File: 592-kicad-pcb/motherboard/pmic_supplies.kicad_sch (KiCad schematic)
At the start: 10 parts, among them U21 MICROCHIP TC1304-VI0EMF, U22 LT1761ES5-BYPTRMPBF

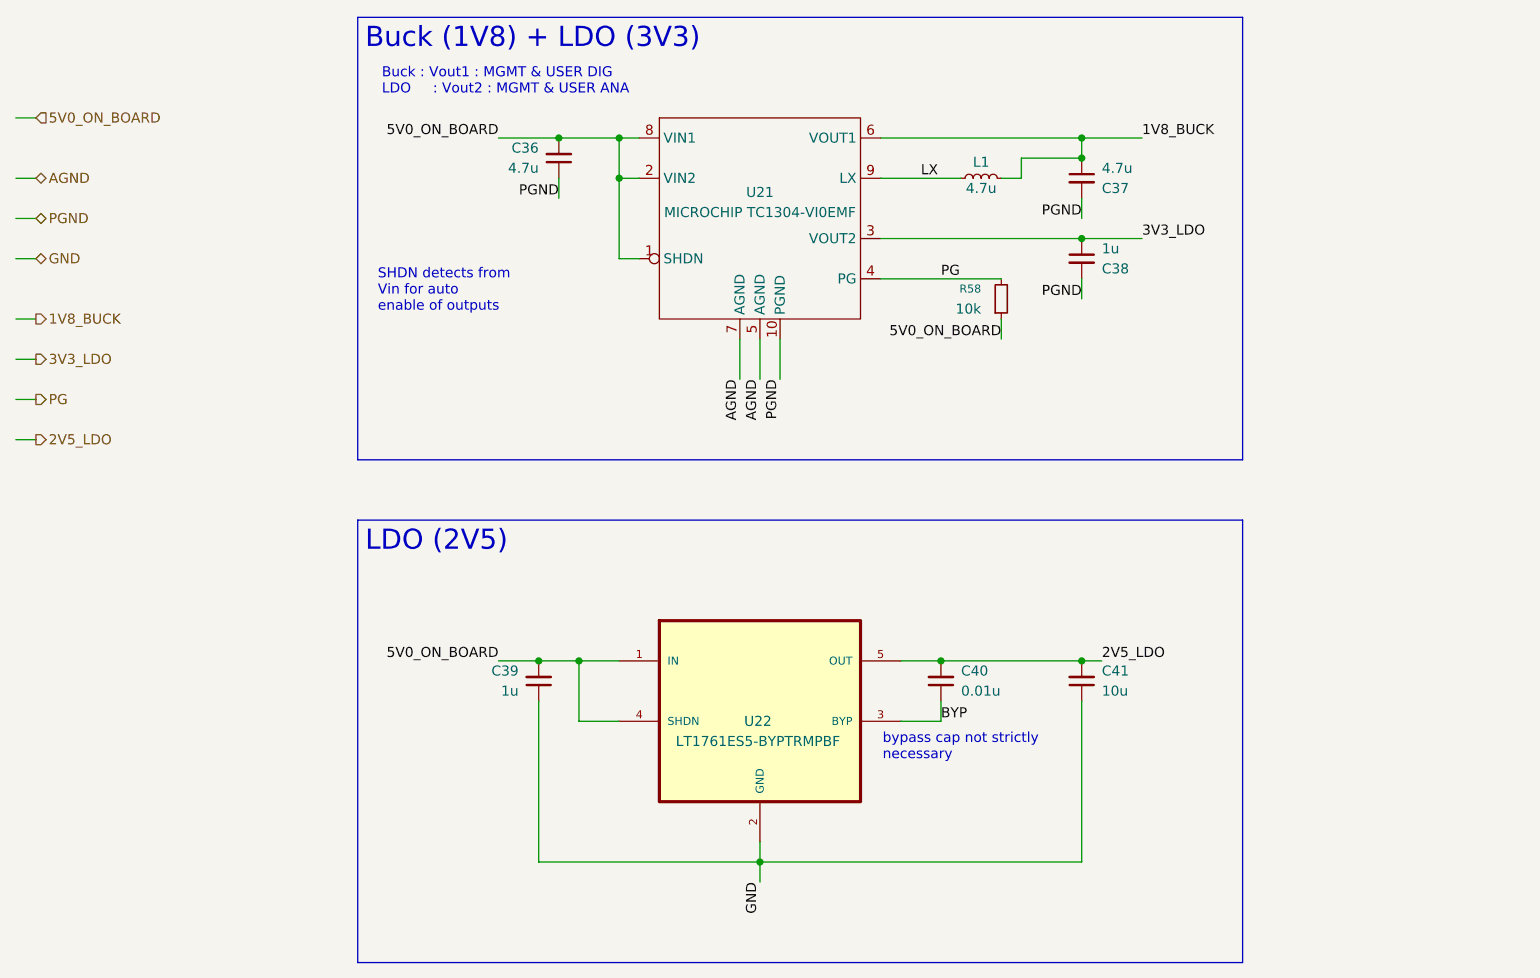
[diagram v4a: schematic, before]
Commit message: fuses, ferrite bead, 5V0 selection connector
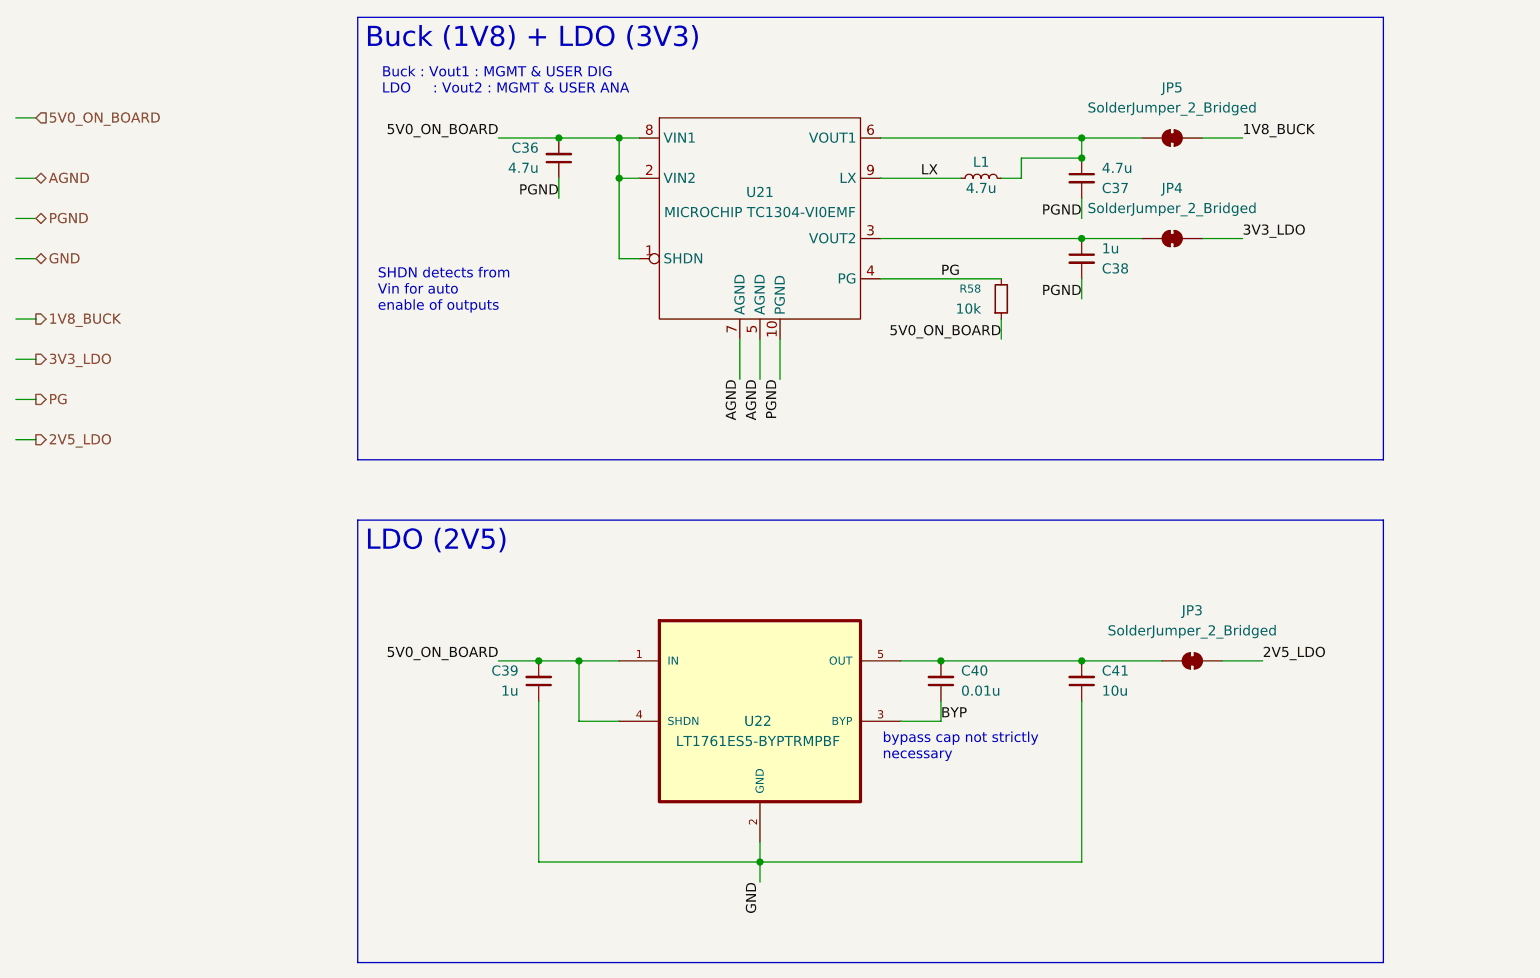
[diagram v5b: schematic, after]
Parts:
- added JP3, JP4, JP5: SolderJumper_2_Bridged, Jumper:SolderJumper-2_P1.3mm_Bridged2Bar_Pad1.0x1.5mm, symbol Jumper:SolderJumper_2_Bridged
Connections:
- net 1V8_BUCK: now also JP5.2 (B); no longer C37.1, L1.2, U21.6 (VOUT1)
- net 2V5_LDO: now also JP3.2 (B); no longer C40.2, C41.2, U22.5 (OUT)
- net 3V3_LDO: now also JP4.2 (B); no longer C38.1, U21.3 (VOUT2)
- new net: C40.2, C41.2, JP3.1 (A), U22.5 (OUT)
- new net: C37.1, JP5.1 (A), L1.2, U21.6 (VOUT1)
- new net: C38.1, JP4.1 (A), U21.3 (VOUT2)
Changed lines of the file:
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@@
 		(exclude_from_sim no)
 		(at 63.5 86.36 0)
-		(size 111.76 55.88)
+		(size 129.54 55.88)
 		(margins 0.9525 0.9525 0.9525 0.9525)
 		(stroke
@@
 		(exclude_from_sim no)
 		(at 63.5 22.86 0)
-		(size 111.76 55.88)
+		(size 129.54 55.88)
 		(margins 0.9525 0.9525 0.9525 0.9525)
 		(stroke
@@
 	(wire
 		(pts
+			(xy 172.72 104.14) (xy 177.8 104.14)
+		)
+		(stroke
+			(width 0)
+			(type default)
+		)
+	)
+	(wire
+		(pts
 			(xy 91.44 104.14) (xy 91.44 111.76)
 		)
@@
 	(wire
 		(pts
-			(xy 154.94 104.14) (xy 157.48 104.14)
+			(xy 154.94 104.14) (xy 165.1 104.14)
 		)
 		(stroke
@@
 	(wire
 		(pts
+			(xy 170.18 50.8) (xy 175.26 50.8)
+		)
+		(stroke
+			(width 0)
+			(type default)
+		)
+	)
+	(wire
+		(pts
 			(xy 96.52 53.34) (xy 99.06 53.34)
 		)
@@
 	(wire
 		(pts
+			(xy 170.18 38.1) (xy 175.26 38.1)
+		)
+		(stroke
+			(width 0)
+			(type default)
+		)
+	)
+	(wire
+		(pts
 			(xy 129.54 50.8) (xy 154.94 50.8)
 		)
@@
 	)
 	(label "3V3_LDO"
-		(at 162.56 50.8 0)
+		(at 175.26 50.8 0)
 		(effects
 			(font
@@
 	)
 	(label "2V5_LDO"
-		(at 157.48 104.14 0)
+		(at 177.8 104.14 0)
 		(effects
 			(font
@@
 	)
 	(label "1V8_BUCK"
-		(at 162.56 38.1 0)
+		(at 175.26 38.1 0)
 		(effects
 			(font
@@
 	)
 	(symbol
+		(lib_id "Jumper:SolderJumper_2_Bridged")
+		(at 166.37 38.1 0)
+		(unit 1)
+		(exclude_from_sim no)
+		(in_bom no)
+		(on_board yes)
+		(dnp no)
+		(fields_autoplaced yes)
+		(property "Reference" "JP5"
+			(at 166.37 31.75 0)
+			(effects
+				(font
+					(size 1.27 1.27)
+				)
+			)
+		)
+		(property "Value" "SolderJumper_2_Bridged"
+			(at 166.37 34.29 0)
+			(effects
+				(font
+					(size 1.27 1.27)
+				)
+			)
+		)
+		(property "Footprint" "Jumper:SolderJumper-2_P1.3mm_Bridged2Bar_Pad1.0x1.5mm"
+			(at 166.37 38.1 0)
+			(effects
+				(font
+					(size 1.27 1.27)
+				)
+				(hide yes)
+			)
+		)
+		(property "Datasheet" "~"
+			(at 166.37 38.1 0)
+			(effects
+				(font
+					(size 1.27 1.27)
+				)
+				(hide yes)
+			)
+		)
+		(property "Description" "Solder Jumper, 2-pole, closed/bridged"
+			(at 166.37 38.1 0)
+			(effects
+				(font
+					(size 1.27 1.27)
+				)
+				(hide yes)
+			)
+		)
+		(pin "2"
+		)
+		(pin "1"
+		)
+		(instances
+			(project "motherboard"
+				(path "/5b0c97ac-fa03-4db8-b41b-0eee32b6f55d/f049e4ad-bebe-4338-850a-2727de737ae9/5cd7239b-a735-4cd0-9e02-9ed9ef16f904"
+					(reference "JP5")
+					(unit 1)
+				)
+			)
+		)
+	)
+	(symbol
 		(lib_id "Device:C_Small")
 		(at 154.94 43.18 0)
@@
 				(path "/5b0c97ac-fa03-4db8-b41b-0eee32b6f55d/f049e4ad-bebe-4338-850a-2727de737ae9/5cd7239b-a735-4cd0-9e02-9ed9ef16f904"
 					(reference "C37")
+					(unit 1)
+				)
+			)
+		)
+	)
+	(symbol
+		(lib_id "Jumper:SolderJumper_2_Bridged")
+		(at 166.37 50.8 0)
+		(unit 1)
+		(exclude_from_sim no)
+		(in_bom no)
+		(on_board yes)
+		(dnp no)
+		(fields_autoplaced yes)
+		(property "Reference" "JP4"
+			(at 166.37 44.45 0)
+			(effects
+				(font
+					(size 1.27 1.27)
+				)
+			)
+		)
+		(property "Value" "SolderJumper_2_Bridged"
+			(at 166.37 46.99 0)
+			(effects
+				(font
+					(size 1.27 1.27)
+				)
+			)
+		)
+		(property "Footprint" "Jumper:SolderJumper-2_P1.3mm_Bridged2Bar_Pad1.0x1.5mm"
+			(at 166.37 50.8 0)
+			(effects
+				(font
+					(size 1.27 1.27)
+				)
+				(hide yes)
+			)
+		)
+		(property "Datasheet" "~"
+			(at 166.37 50.8 0)
+			(effects
+				(font
+					(size 1.27 1.27)
+				)
+				(hide yes)
+			)
+		)
+		(property "Description" "Solder Jumper, 2-pole, closed/bridged"
+			(at 166.37 50.8 0)
+			(effects
+				(font
+					(size 1.27 1.27)
+				)
+				(hide yes)
+			)
+		)
+		(pin "2"
+		)
+		(pin "1"
+		)
+		(instances
+			(project "motherboard"
+				(path "/5b0c97ac-fa03-4db8-b41b-0eee32b6f55d/f049e4ad-bebe-4338-850a-2727de737ae9/5cd7239b-a735-4cd0-9e02-9ed9ef16f904"
+					(reference "JP4")
 					(unit 1)
 				)
@@
 					(unit 1)
 				)
+			)
+		)
+	)
+	(symbol
+		(lib_id "Jumper:SolderJumper_2_Bridged")
+		(at 168.91 104.14 0)
+		(unit 1)
+		(exclude_from_sim no)
+		(in_bom no)
+		(on_board yes)
+		(dnp no)
+		(fields_autoplaced yes)
+		(property "Reference" "JP3"
+			(at 168.91 97.79 0)
+			(effects
+				(font
+					(size 1.27 1.27)
+				)
+			)
+		)
+		(property "Value" "SolderJumper_2_Bridged"
+			(at 168.91 100.33 0)
+			(effects
+				(font
+					(size 1.27 1.27)
+				)
+			)
+		)
+		(property "Footprint" "Jumper:SolderJumper-2_P1.3mm_Bridged2Bar_Pad1.0x1.5mm"
+			(at 168.91 104.14 0)
+			(effects
+				(font
+					(size 1.27 1.27)
+				)
+				(hide yes)
+			)
+		)
+		(property "Datasheet" "~"
+			(at 168.91 104.14 0)
+			(effects
+				(font
+					(size 1.27 1.27)
+				)
+				(hide yes)
+			)
+		)
+		(property "Description" "Solder Jumper, 2-pole, closed/bridged"
+			(at 168.91 104.14 0)
+			(effects
+				(font
+					(size 1.27 1.27)
+				)
+				(hide yes)
+			)
+		)
+		(pin "2"
+		)
+		(pin "1"
+		)
+		(instances
+			(project ""
+				(path "/5b0c97ac-fa03-4db8-b41b-0eee32b6f55d/f049e4ad-bebe-4338-850a-2727de737ae9/5cd7239b-a735-4cd0-9e02-9ed9ef16f904"
+					(reference "JP3")
+					(unit 1)
+				)

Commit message: supply connectors, solder bridges
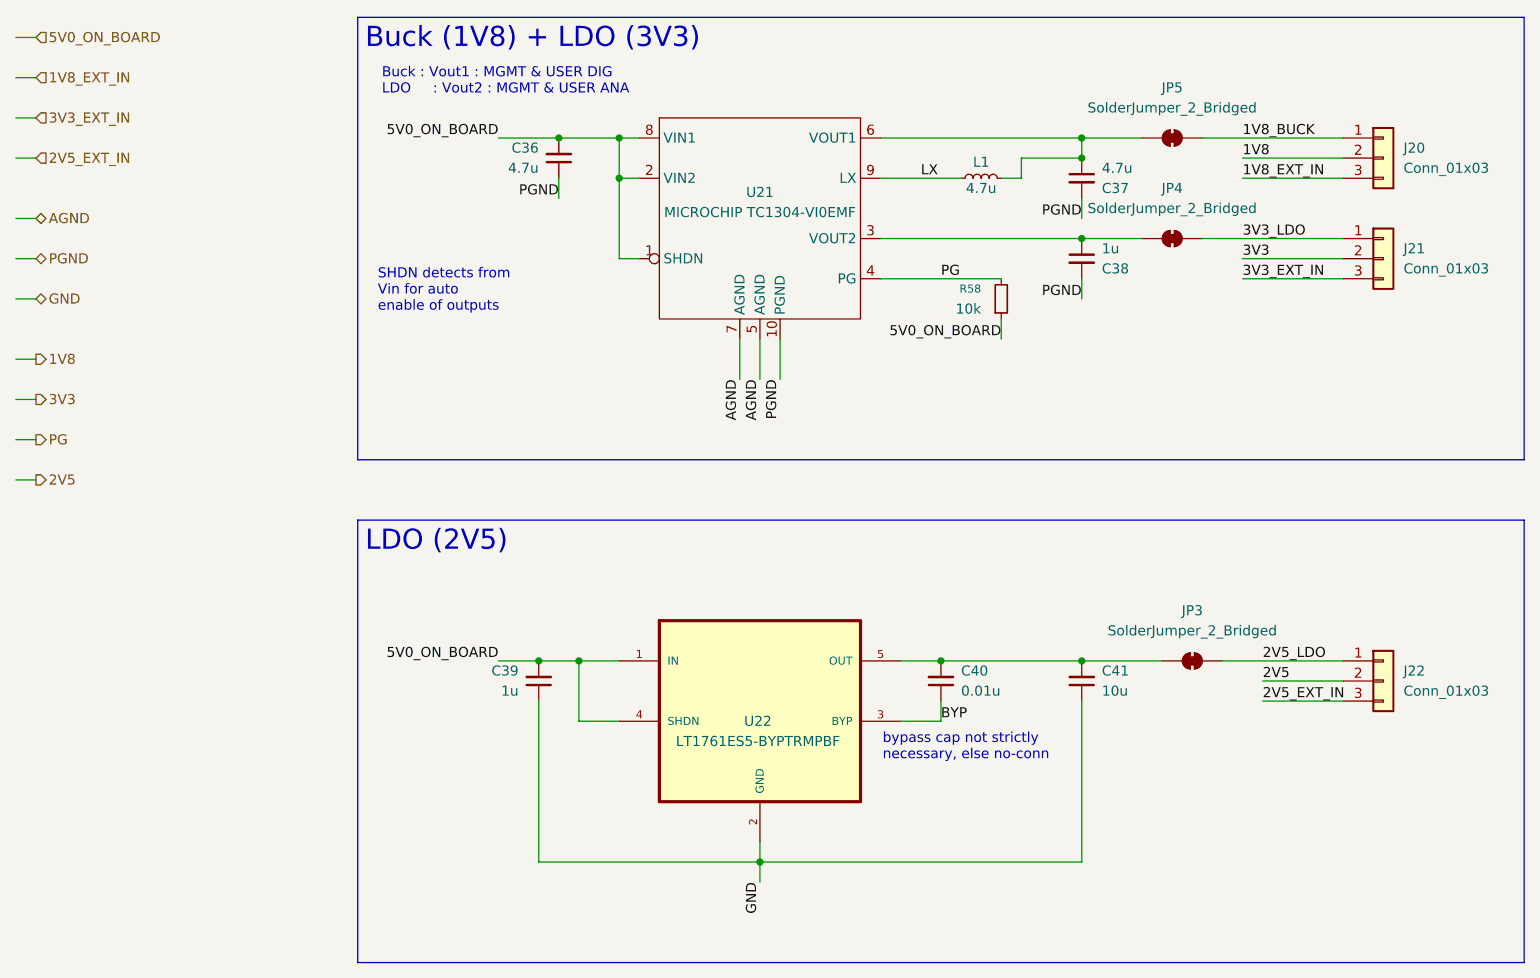
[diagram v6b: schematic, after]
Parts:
- added J20, J21, J22: Conn_01x03, symbol Connector_Generic:Conn_01x03
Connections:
- net 1V8_BUCK: now also J20.1 (Pin_1)
- net 2V5_LDO: now also J22.1 (Pin_1)
- net 3V3_LDO: now also J21.1 (Pin_1)
- new net 1V8: J20.2 (Pin_2)
- new net 1V8_EXT_IN: J20.3 (Pin_3)
- new net 2V5: J22.2 (Pin_2)
- new net 2V5_EXT_IN: J22.3 (Pin_3)
- new net 3V3: J21.2 (Pin_2)
- new net 3V3_EXT_IN: J21.3 (Pin_3)
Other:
- note added: "bypass cap not strictly necessary, else no-conn"
- note removed: "bypass cap not strictly necessary"
